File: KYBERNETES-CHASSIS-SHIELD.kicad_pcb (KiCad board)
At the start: 4 copper layers, 53.8 x 67.1 mm, 42 parts, among them J1 ESC, J10 Fan, J2 Radio, J3 Encoder, J4 I2C, J5 Bumper, J6 Servo 1, J7 Servo 2, J8 Servo Regulator 1, J9 Servo Regulator 2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

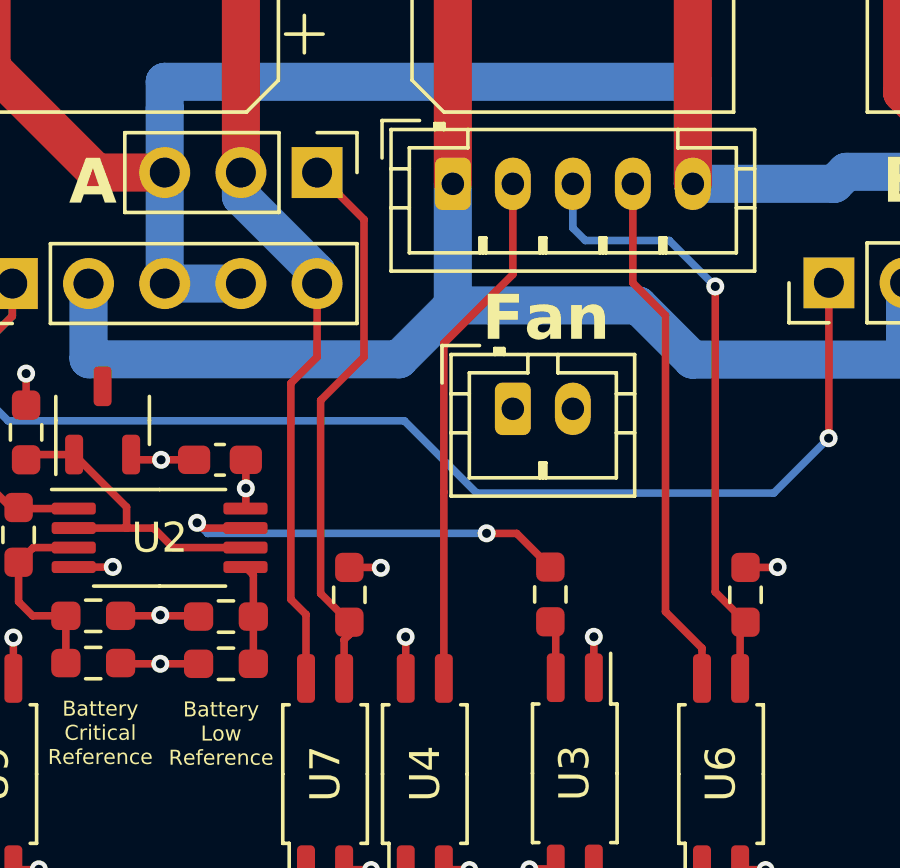
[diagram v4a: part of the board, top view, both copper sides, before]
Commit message: add a mosfet after the esc enable opto to as it is not just an enable line as previously thought. needs more current than opto can provide.
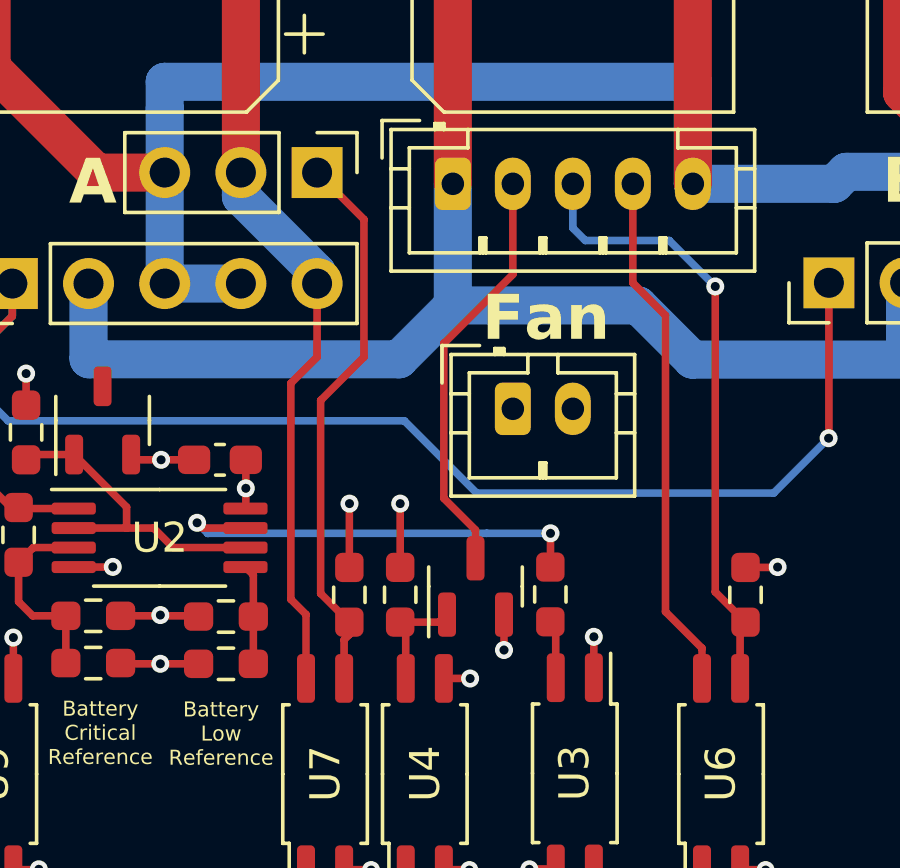
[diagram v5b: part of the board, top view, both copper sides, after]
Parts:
- added Q1: Si2393DS, Package_TO_SOT_SMD:SOT-23, F.Cu at (148.5, 91.4)
- added R16: 2k2, Resistor_SMD:R_0603_1608Metric_Pad0.98x0.95mm_HandSolder, F.Cu at (146.0, 91.6)
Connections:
- U4 pad 3: ESC_ENABLE -> GND2
- U4 pad 4: +12V -> Net-(Q1-G)
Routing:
- net Net-(Q1-G): track 0.00 -> 3.62 mm
- net ESC_ENABLE: track 17.4 -> 13.9 mm
- net GND2: track 84.3 -> 86.3 mm, vias 7 -> 8
- net +12V: track 53.7 -> 55.6 mm, vias 5 -> 6
- net Net-(R6-Pad1): track 14.1 -> 14.7 mm

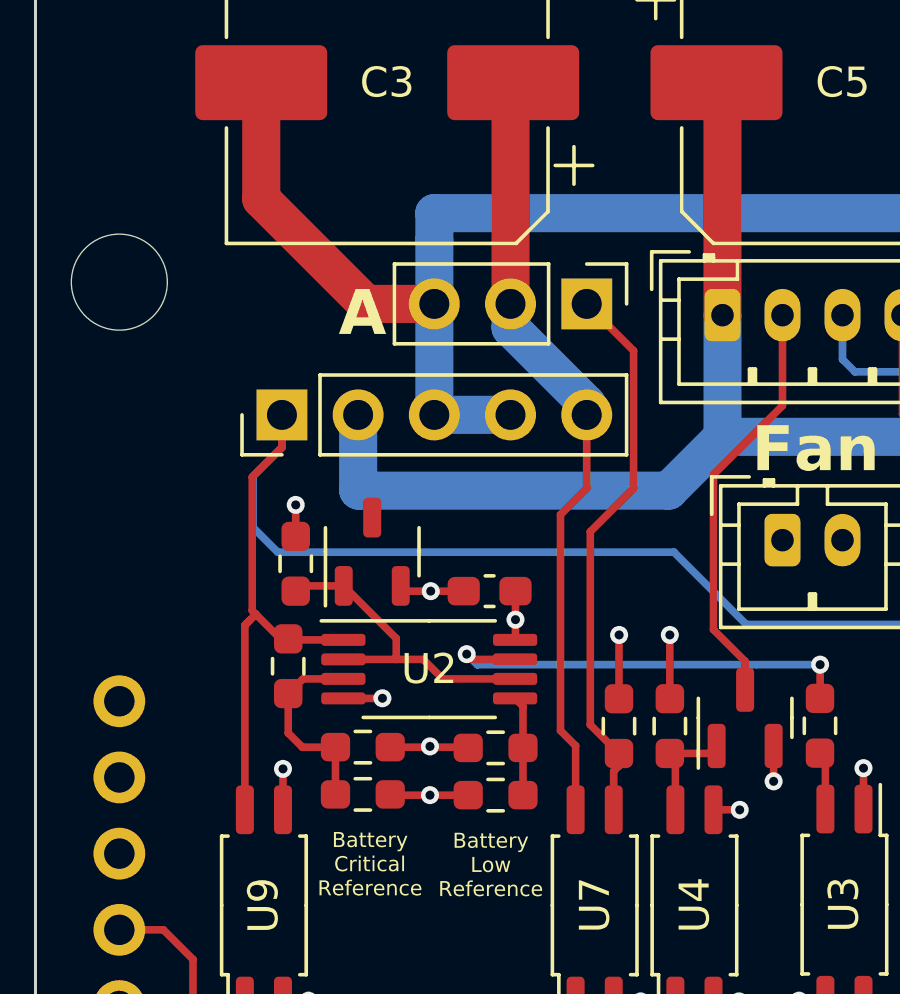
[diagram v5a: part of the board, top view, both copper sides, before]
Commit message: change the servo enable optoisolator to a high side switch
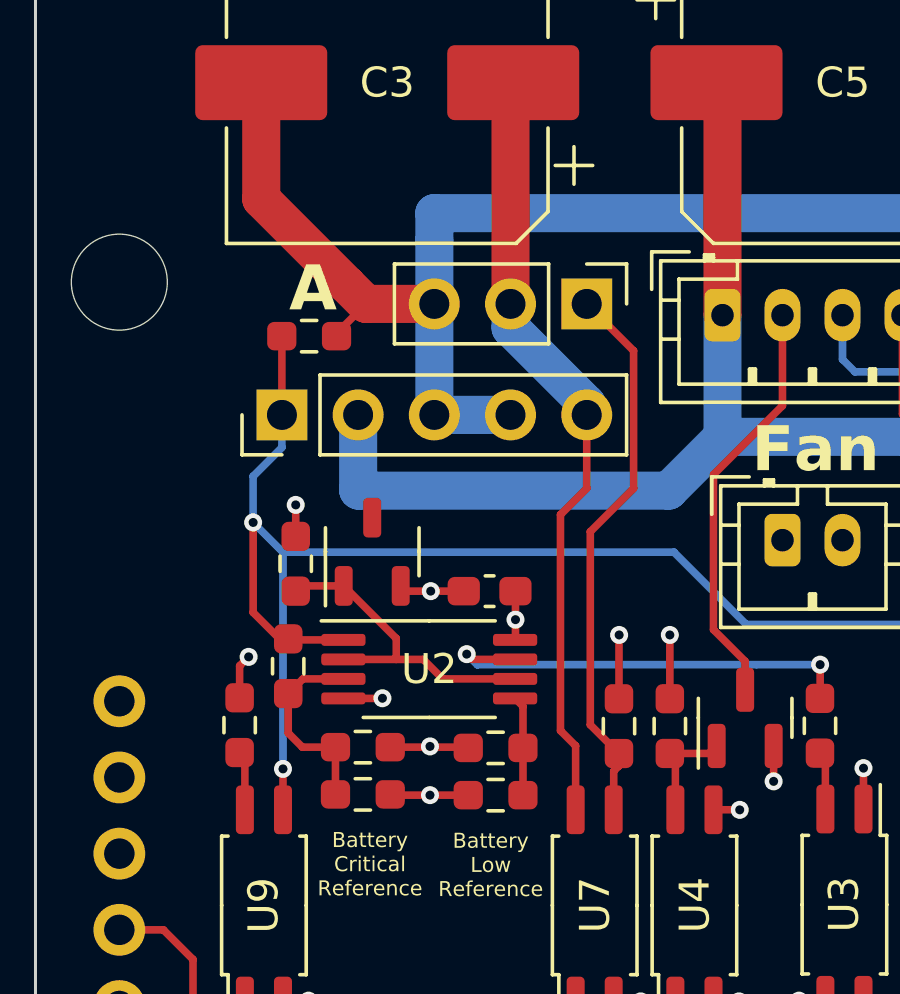
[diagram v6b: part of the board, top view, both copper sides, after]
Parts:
- added R17: 10k, Resistor_SMD:R_0603_1608Metric_Pad0.98x0.95mm_HandSolder, F.Cu at (131.7, 91.6)
- added R20: 100k, Resistor_SMD:R_0603_1608Metric_Pad0.98x0.95mm_HandSolder, F.Cu at (134.0, 78.7)
- R16: value 2k2 -> 10k
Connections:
- net SERVO_DISABLE_LOGIC renamed SERVO_ENABLE_LOGIC
- J8 pad 1: SERVO_DISABLE -> SERVO_ENABLE
- J9 pad 1: SERVO_DISABLE -> SERVO_ENABLE
- R15 pad 2: SERVO_DISABLE -> SERVO_ENABLE
- U2 pad 1: SERVO_DISABLE -> SERVO_ENABLE
- U9 pad 3: GND2 -> SERVO_ENABLE
- U9 pad 4: SERVO_DISABLE -> Net-(R17-Pad2)
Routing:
- net SERVO_ENABLE: track 0.00 -> 57.4 mm, vias 0 -> 3
- net SERVO_DISABLE: track 56.9 -> 0.00 mm, vias 1 -> 0
- net Net-(R17-Pad2): track 0.00 -> 1.98 mm
- net +12V: track 55.6 -> 57.1 mm, vias 6 -> 7
- net GND2: track 86.3 -> 86.4 mm, vias 8 -> 7
